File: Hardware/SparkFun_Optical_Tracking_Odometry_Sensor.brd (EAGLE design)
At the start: 25.4 x 25.4 mm, 71 parts, among them J1 QWIIC_RIGHT_ANGLE, J2 QWIIC_RIGHT_ANGLE, U1 PAA5160, U2 LSM6DS0, U3 STM32C011F4U6, U4 RT9080-33GJ5

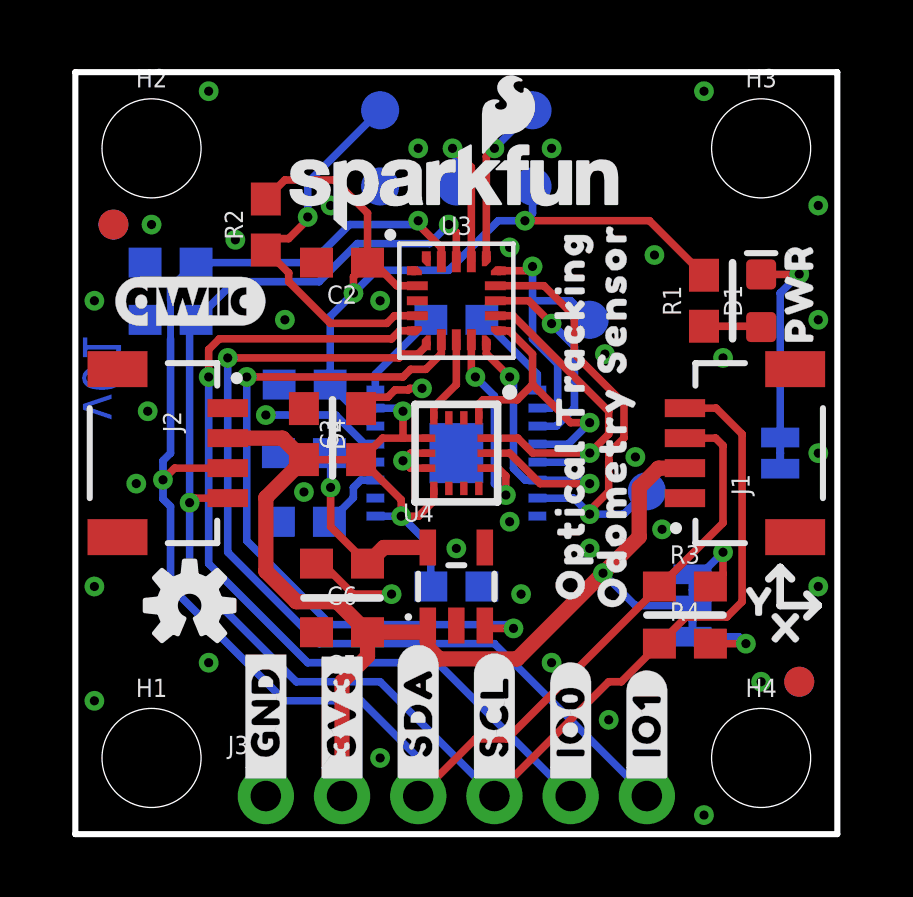
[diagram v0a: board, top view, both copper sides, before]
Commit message: PAA5160 footprint tweaks
Adjust pads to match datasheet recommendations
Reduce silk outline to be only in corners
Add tDocu lines for sensor location and pin 1 indication

Also remove pullup resistor on the STM reset net, the STM has an internal pullup
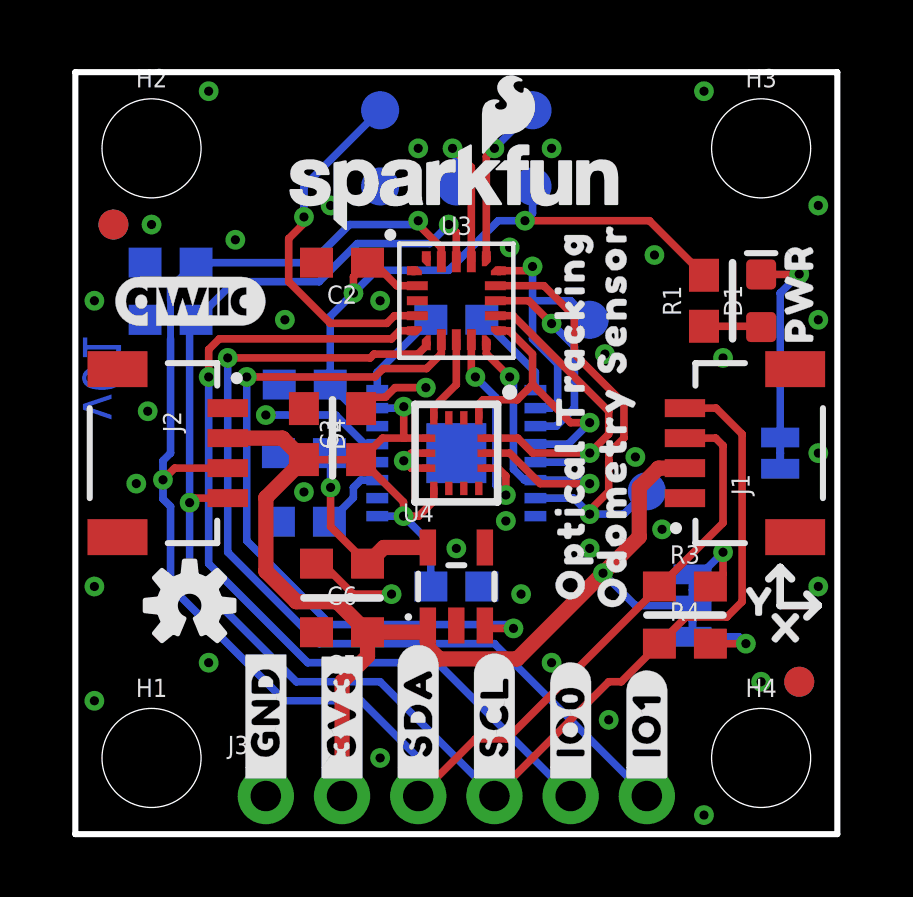
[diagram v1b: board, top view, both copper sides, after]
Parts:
- removed R2: 10k, SparkFun-Resistors:0603
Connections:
- net 3.3V: no longer R2.2
- net STM_!RST!: no longer R2.1
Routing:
- net 3.3V: track 78.8 -> 73.1 mm
- net STM_!RST!: track 12.8 -> 11.9 mm

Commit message: v02 update
Add MOSFETs controlled by GPIO pins in order to supply power to PAA5160 with correct timings
Add correct decoupling capacitors
Rearrange some GPIO pins
Reduce silk around STM32C0
Reroute entire board 🙃
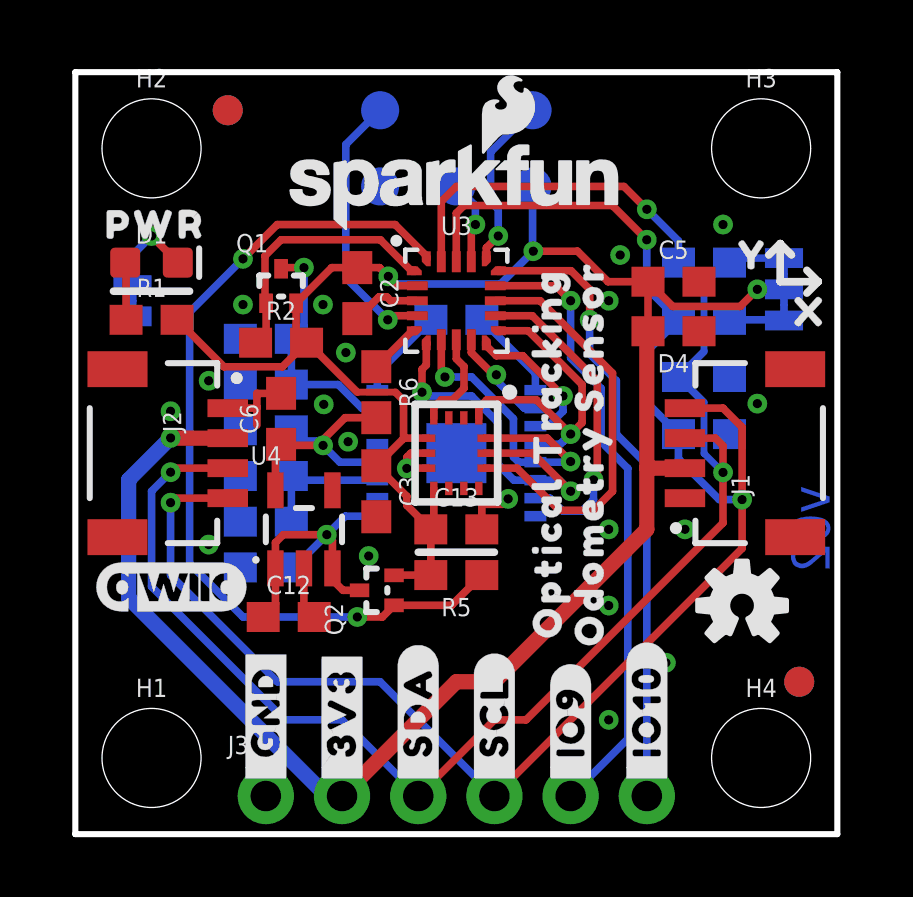
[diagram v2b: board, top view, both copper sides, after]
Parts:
- removed TP1, TP2: TEST-POINT3X5, SparkFun-Connectors:PAD.03X.05
- removed U$23: (no value), output:LASER0
- added C10, C11: 4.7uF, SparkFun-Capacitors:0603
- added C12: 22uF, SparkFun-Capacitors:0603
- added C13: 0.1uF, SparkFun-Capacitors:0603
- added Q1, Q2: 100mA/20V/3.8Ω, SparkFun-DiscreteSemi:SOT-416FL
- added R2, R5, R6: 100k, SparkFun-Resistors:0603
- C5, C6: value 10uF -> 22uF
- U$12: device output:#_IO0#0 -> output:#_IO9#0
- U$13: device output:#_IO1#0 -> output:#IO10_#0
- U$19: device output:CLASS_10 -> output:#IO9_#0
- U$6: device output:#_IO0#0 -> output:CLASS_1_LASER0
- U$7: device output:#_IO1#0 -> output:#_IO10#0
- moved PWR 22.2 mm to (1.91, 17.8)
- moved U$20 22.2 mm to (1.91, 16.9)
- moved U$24 21.6 mm to (2.54, 7.62)
- moved U$25 21.6 mm to (2.67, 20.3), turned to 0 degrees
- moved D1 20.4 mm to (2.54, 19.1), turned to 0 degrees
- moved R1 18.4 mm to (2.54, 17.1), turned to 0 degrees
- moved LOGO1 18.4 mm to (22.2, 7.62)
- moved D2 18.2 mm to (21.0, 15.2), turned to 0 degrees
- moved D3 18.2 mm to (21.0, 13.3), turned to 0 degrees
- moved C5 16.1 mm to (19.9, 18.4), turned to 0 degrees
- moved U$19 15.7 mm to (16.5, 1.52), turned to 270 degrees
- moved D4 12.8 mm to (19.9, 16.8), turned to 180 degrees
- moved U$29 11.6 mm to (22.6, 19.3)
- moved I2C 11.0 mm to (23.6, 18.2)
- moved R3 10.8 mm to (21.0, 19.1), flipped to the bottom, turned to 180 degrees
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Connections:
- removed net 1V8_EN: U3.7, U4.3
- removed net STM_IO0: J3.5, U3.5
- removed net STM_IO1: J3.6, U3.6
- new net !PAA_POW!: Q2.1, R5.1, U3.20
- new net !VCSEL_POW!: Q1.1, R2.1, U3.1
- new net 3.3V_SW: C12.1, C8.1, Q2.3, U1.9, U4.1, U4.3
- new net 3.3V_SW2: C10.1, C4.1, Q1.3, U1.15
- new net N$8: R6.1, U3.5
- new net STM_IO10: J3.6, U3.15
- new net STM_IO9: J3.5, U3.14
- net 1.8V: now also R6.2
- net 3.3V: now also C13.1, Q1.2, Q2.2, R2.2, R5.2; no longer C4.1, C8.1, U1.15, U1.9, U4.1
- net GND: now also C10.2, C11.2, C12.2, C13.2
- net LSM_!CS!: now also U3.13; no longer U3.9
- net N$7: now also C11.1
- net PAA_!CS!: now also U3.10; no longer U3.13
- net PAA_!RST!: now also U3.9; no longer TP2.1, U3.15
- net PAA_MOTION: now also U3.12; no longer TP1.1, U3.14
- net PICO: now also U3.7; no longer U3.12
- net SCK: now also U3.6; no longer U3.10
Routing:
- net STM_IO1: track 30.6 -> 0.00 mm, vias 1 -> 0
- net STM_IO0: track 29.4 -> 0.00 mm, vias 1 -> 0
- net !PAA_POW!: track 0.00 -> 29.0 mm, vias 0 -> 2
- net 1V8_EN: track 23.8 -> 0.00 mm, vias 2 -> 0
- net STM_IO10: track 0.00 -> 20.9 mm, vias 0 -> 1
- net STM_IO9: track 0.00 -> 20.8 mm, vias 0 -> 1
- net 3.3V: track 73.1 -> 84.0 mm, vias 5 -> 4
- net 3.3V_SW: track 0.00 -> 10.7 mm, vias 0 -> 1
- net !VCSEL_POW!: track 0.00 -> 8.58 mm
- net 3.3V_SW2: track 0.00 -> 8.04 mm, vias 0 -> 1
- net LSM_!CS!: track 7.12 -> 14.0 mm, vias 2 -> 0
- net PAA_!RST!: track 8.95 -> 3.44 mm
- net PAA_MOTION: track 15.1 -> 10.6 mm
- net N$2: track 6.99 -> 3.15 mm
- net SCL: track 53.0 -> 55.9 mm, vias 2 -> 3
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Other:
- board text added: "v02"
- board text removed: "v01"

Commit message: Improve GND pour
Add GND vias
Nudge via locations to dodge silkscreen better
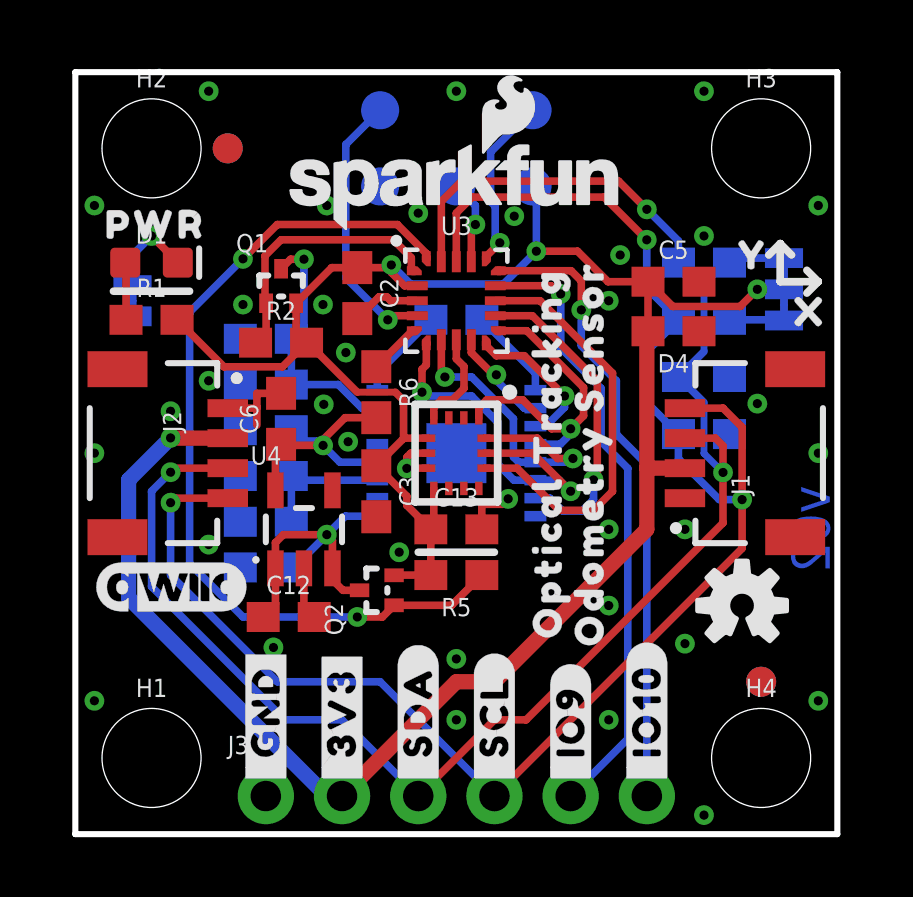
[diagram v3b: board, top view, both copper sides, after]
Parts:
- moved FD1 1.27 mm to (5.08, 22.9)
- moved FD2 1.27 mm to (5.08, 22.9)
- moved FD3 1.27 mm to (22.9, 5.08)
- moved FD4 1.27 mm to (22.9, 5.08)
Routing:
- net GND: vias 20 -> 36

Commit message: Design review updates
Add regulator name to section in schematic
Add voltage ranges for each component, and required voltage range for entire board
Add GND via next to STM32 GND pad
Center traces between Q1 and R2
Nudge via and 3.3V trace left of R6 to get better GND stitching
Fix acid trap with via under U4
Fix orientation of silk on bottom
Add silk line between D4 and C5
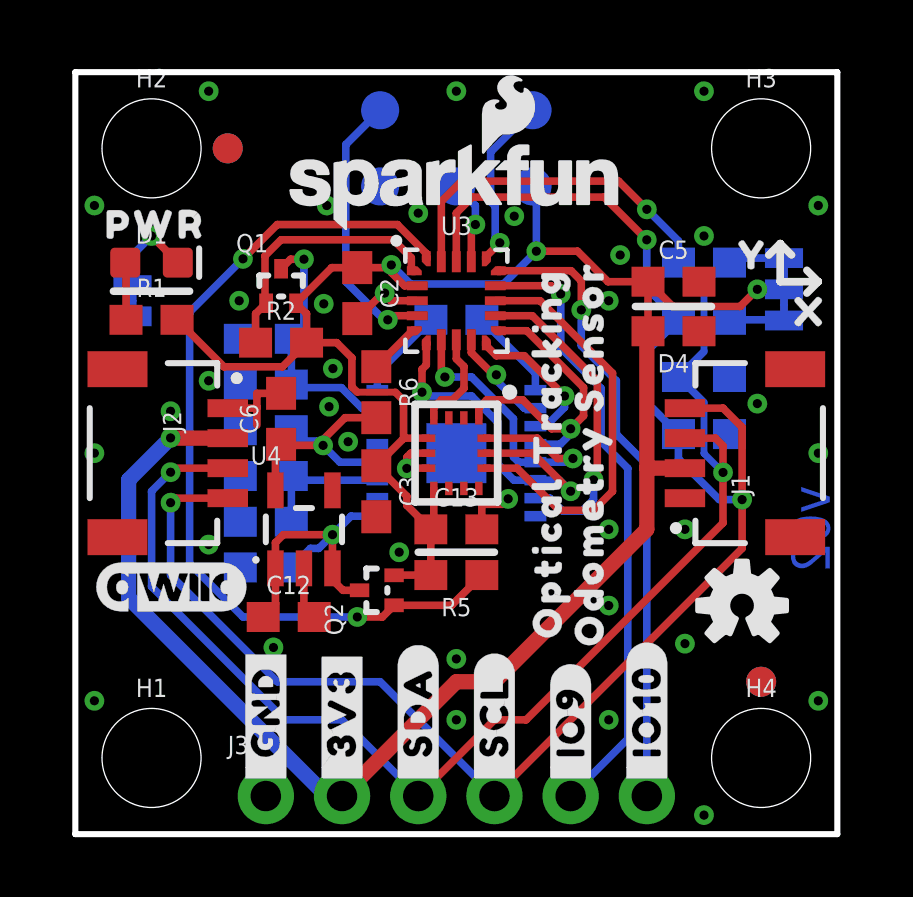
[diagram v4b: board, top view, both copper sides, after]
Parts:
- removed U$13: (no value), output:#IO10_#0
- removed U$19: (no value), output:#IO9_#0
- added U$23: (no value), output:#_IO10#0
- added U$32: (no value), output:#_IO9#0
- turned U$26 to 90 degrees
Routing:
- net 3.3V: track 84.3 -> 84.9 mm
- net GND: vias 36 -> 37
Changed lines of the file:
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@@
 <dimension x1="12.7" y1="12.7" x2="12.7" y2="0" x3="-5.08" y3="6.35" textsize="1.778" textratio="15" layer="47" unit="inch"/>
 <dimension x1="19.05" y1="1.27" x2="19.05" y2="0" x3="-1.27" y3="0.635" textsize="1.778" textratio="15" layer="47" unit="inch"/>
+<wire x1="18.669" y1="17.5895" x2="21.209" y2="17.5895" width="0.254" layer="21"/>
 </plain>
 <attributes>
@@
 <attribute name="VALUE" x="20.955" y="17.907" size="0.6096" layer="28" font="vector" ratio="20" rot="MR180" align="top-center"/>
 </element>
-<element name="U$26" library="output" package="#I2C#0" value="" x="23.622" y="16.764" smashed="yes" rot="MR270"/>
+<element name="U$26" library="output" package="#I2C#0" value="" x="23.622" y="16.764" smashed="yes" rot="MR90"/>
 <element name="D2" library="SparkFun-DiscreteSemi" package="0603" value="24V" x="20.955" y="15.24" smashed="yes" rot="MR0">
 <attribute name="NAME" x="20.955" y="16.002" size="0.6096" layer="26" font="vector" ratio="20" rot="MR0" align="bottom-center"/>
@@
 <element name="U$12" library="output" package="#_IO9#0" value="" x="16.51" y="1.524" smashed="yes" rot="R90"/>
 <element name="U$7" library="output" package="#_IO10#0" value="" x="19.05" y="1.524" smashed="yes" rot="R90"/>
-<element name="U$13" library="output" package="#IO10_#0" value="" x="19.05" y="1.524" smashed="yes" rot="MR270"/>
-<element name="U$19" library="output" package="#IO9_#0" value="" x="16.51" y="1.524" smashed="yes" rot="MR270"/>
 <element name="C5" library="SparkFun-Capacitors" package="0603" value="22uF" x="19.939" y="18.415" smashed="yes">
 <attribute name="NAME" x="19.939" y="19.177" size="0.6096" layer="25" font="vector" ratio="20" align="bottom-center"/>
@@
 <attribute name="VALUE" x="19.939" y="17.653" size="0.6096" layer="27" font="vector" ratio="20" align="top-center"/>
 </element>
+<element name="U$23" library="output" package="#_IO10#0" value="" x="19.05" y="1.524" smashed="yes" rot="MR90"/>
+<element name="U$32" library="output" package="#_IO9#0" value="" x="16.51" y="1.524" smashed="yes" rot="MR90"/>
 </elements>
 <signals>
@@
 <via x="4.445" y="9.652" extent="1-16" drill="0.3048"/>
 <via x="3.175" y="14.097" extent="1-16" drill="0.3048"/>
-<via x="9.017" y="16.0528" extent="1-16" drill="0.3048"/>
-<via x="8.2804" y="14.3256" extent="1-16" drill="0.3048"/>
+<via x="8.5852" y="15.5194" extent="1-16" drill="0.3048"/>
+<via x="8.4582" y="14.2494" extent="1-16" drill="0.3048"/>
 <via x="10.795" y="9.398" extent="1-16" drill="0.3048"/>
-<via x="5.588" y="17.653" extent="1-16" drill="0.3048"/>
-<via x="8.255" y="17.653" extent="1-16" drill="0.3048"/>
+<via x="5.461" y="17.78" extent="1-16" drill="0.3048"/>
+<via x="8.2804" y="17.6784" extent="1-16" drill="0.3048"/>
 <wire x1="6.858" y1="14.693" x2="6.0532" y2="14.693" width="0.254" layer="1"/>
 <wire x1="6.0532" y1="14.693" x2="6.0532" y2="14.224" width="0.254" layer="1"/>
@@
 <via x="12.7" y="3.81" extent="1-16" drill="0.3048"/>
 <via x="12.7" y="5.842" extent="1-16" drill="0.3048"/>
+<via x="10.3124" y="18.034" extent="1-16" drill="0.3048"/>
 </signal>
 <signal name="1.8V">
@@
 <wire x1="10.633" y1="8.636" x2="11.85" y2="8.636" width="0.254" layer="1"/>
 <wire x1="11.85" y1="8.636" x2="11.85" y2="10.16" width="0.254" layer="1"/>
-<wire x1="7.747" y1="16.383" x2="7.708" y2="16.383" width="0.254" layer="1"/>
-<wire x1="9.398" y1="14.732" x2="7.747" y2="16.383" width="0.254" layer="1"/>
-<wire x1="7.358" y1="17.696" x2="7.358" y2="16.733" width="0.254" layer="1"/>
-<wire x1="7.358" y1="16.733" x2="7.708" y2="16.383" width="0.254" layer="1"/>
+<wire x1="9.398" y1="14.732" x2="9.2202" y2="14.9098" width="0.254" layer="1"/>
+<wire x1="7.358" y1="17.696" x2="7.708" y2="17.346" width="0.254" layer="1"/>
+<wire x1="7.708" y1="17.346" x2="7.708" y2="16.383" width="0.254" layer="1"/>
 <wire x1="7.358" y1="17.696" x2="8.546" y2="18.884" width="0.254" layer="1"/>
 <wire x1="8.546" y1="18.884" x2="9.398" y2="18.884" width="0.254" layer="1"/>
@@
 <wire x1="17.7556625" y1="18.415" x2="16.7396625" y2="19.431" width="0.254" layer="1"/>
 <wire x1="16.7396625" y1="19.431" x2="15.367" y2="19.431" width="0.254" layer="1"/>
+<wire x1="9.2202" y1="14.9098" x2="9.2202" y2="15.875" width="0.254" layer="1"/>
+<wire x1="8.7122" y1="16.383" x2="7.708" y2="16.383" width="0.254" layer="1"/>
+<wire x1="9.2202" y1="15.875" x2="8.7122" y2="16.383" width="0.254" layer="1"/>
 </signal>
 <signal name="LSM_!CS!">
@@
 <wire x1="10.549" y1="17.28" x2="10.414" y2="17.145" width="0.254" layer="1"/>
 <via x="10.414" y="17.145" extent="1-16" drill="0.3048"/>
-<wire x1="10.414" y1="17.145" x2="9.017" y2="18.542" width="0.254" layer="16"/>
+<wire x1="10.414" y1="17.145" x2="10.287" y2="17.145" width="0.254" layer="16"/>
+<wire x1="10.287" y1="17.145" x2="9.017" y2="18.415" width="0.254" layer="16"/>
 <wire x1="10.16" y1="24.13" x2="9.017" y2="22.987" width="0.254" layer="16"/>
-<wire x1="9.017" y1="22.987" x2="9.017" y2="18.542" width="0.254" layer="16"/>
+<wire x1="9.017" y1="22.987" x2="9.017" y2="18.415" width="0.254" layer="16"/>
 </signal>
 <signal name="STM_SWDIO">
@@
 <wire x1="11.2" y1="18.78" x2="11.2" y2="19.2118" width="0.254" layer="1"/>
 <wire x1="11.2" y1="19.2118" x2="10.5998" y2="19.812" width="0.254" layer="1"/>
-<wire x1="6.008" y1="16.383" x2="6.358" y2="16.733" width="0.254" layer="1"/>
-<wire x1="6.358" y1="16.733" x2="6.358" y2="17.696" width="0.254" layer="1"/>
+<wire x1="6.008" y1="17.346" x2="6.008" y2="16.383" width="0.254" layer="1"/>
+<wire x1="6.008" y1="17.346" x2="6.358" y2="17.696" width="0.254" layer="1"/>
 <wire x1="6.858" y1="19.812" x2="10.5998" y2="19.812" width="0.254" layer="1"/>
 <wire x1="6.358" y1="17.696" x2="6.3232" y2="17.7308" width="0.254" layer="1"/>
@@
 <contactref element="U1" pad="15"/>
 <contactref element="C4" pad="1"/>
-<wire x1="7.2" y1="14.986" x2="8.763" y2="14.986" width="0.254" layer="16"/>
-<wire x1="8.763" y1="14.986" x2="9.549" y2="14.2" width="0.254" layer="16"/>
+<wire x1="8.8646" y1="14.8844" x2="7.3016" y2="14.8844" width="0.254" layer="16"/>
+<wire x1="7.2" y1="14.986" x2="7.3016" y2="14.8844" width="0.254" layer="16"/>
+<wire x1="8.8646" y1="14.8844" x2="9.549" y2="14.2" width="0.254" layer="16"/>
 <wire x1="9.549" y1="14.2" x2="10.065" y2="14.2" width="0.254" layer="16"/>
 <wire x1="7.2" y1="16.51" x2="7.2" y2="14.986" width="0.254" layer="16"/>
@@
 <wire x1="8.9209" y1="8.128" x2="8.57" y2="8.4789" width="0.254" layer="1"/>
 <wire x1="8.57" y1="8.4789" x2="8.57" y2="8.8599" width="0.254" layer="1"/>
-<wire x1="8.57" y1="8.8599" x2="8.57" y2="9.7942" width="0.254" layer="1"/>
-<wire x1="8.57" y1="9.7942" x2="8.382" y2="9.9822" width="0.254" layer="1"/>
-<via x="8.382" y="9.9822" extent="1-16" drill="0.3048"/>
+<wire x1="8.57" y1="8.8599" x2="8.57" y2="9.9797" width="0.254" layer="1"/>
+<wire x1="8.57" y1="9.9797" x2="8.5725" y2="9.9822" width="0.254" layer="1"/>
+<via x="8.5725" y="9.9822" extent="1-16" drill="0.3048"/>
 <wire x1="6.67" y1="8.8599" x2="6.67" y2="9.718" width="0.254" layer="1"/>
-<wire x1="6.9342" y1="9.9822" x2="8.382" y2="9.9822" width="0.254" layer="1"/>
+<wire x1="6.9342" y1="9.9822" x2="8.5725" y2="9.9822" width="0.254" layer="1"/>
 <wire x1="6.67" y1="9.718" x2="6.9342" y2="9.9822" width="0.254" layer="1"/>
-<wire x1="7.2" y1="8.89" x2="7.2898" y2="8.89" width="0.254" layer="16"/>
-<wire x1="7.2898" y1="8.89" x2="8.382" y2="9.9822" width="0.254" layer="16"/>
-<wire x1="8.382" y1="9.9822" x2="8.9998" y2="10.6" width="0.254" layer="16"/>
-<wire x1="8.9998" y1="10.6" x2="10.065" y2="10.6" width="0.254" layer="16"/>
+<wire x1="7.2" y1="8.89" x2="7.835" y2="9.525" width="0.254" layer="16"/>
+<wire x1="8.1153" y1="9.525" x2="7.835" y2="9.525" width="0.254" layer="16"/>
+<wire x1="8.1153" y1="9.525" x2="8.5725" y2="9.9822" width="0.254" layer="16"/>
+<wire x1="8.5725" y1="9.9822" x2="9.1903" y2="10.6" width="0.254" layer="16"/>
+<wire x1="9.1903" y1="10.6" x2="10.065" y2="10.6" width="0.254" layer="16"/>
 </signal>
 <signal name="!PAA_POW!">
